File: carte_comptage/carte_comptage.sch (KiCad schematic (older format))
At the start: 40 parts, among them Q1 Si2302DS, U33 AP1117-33

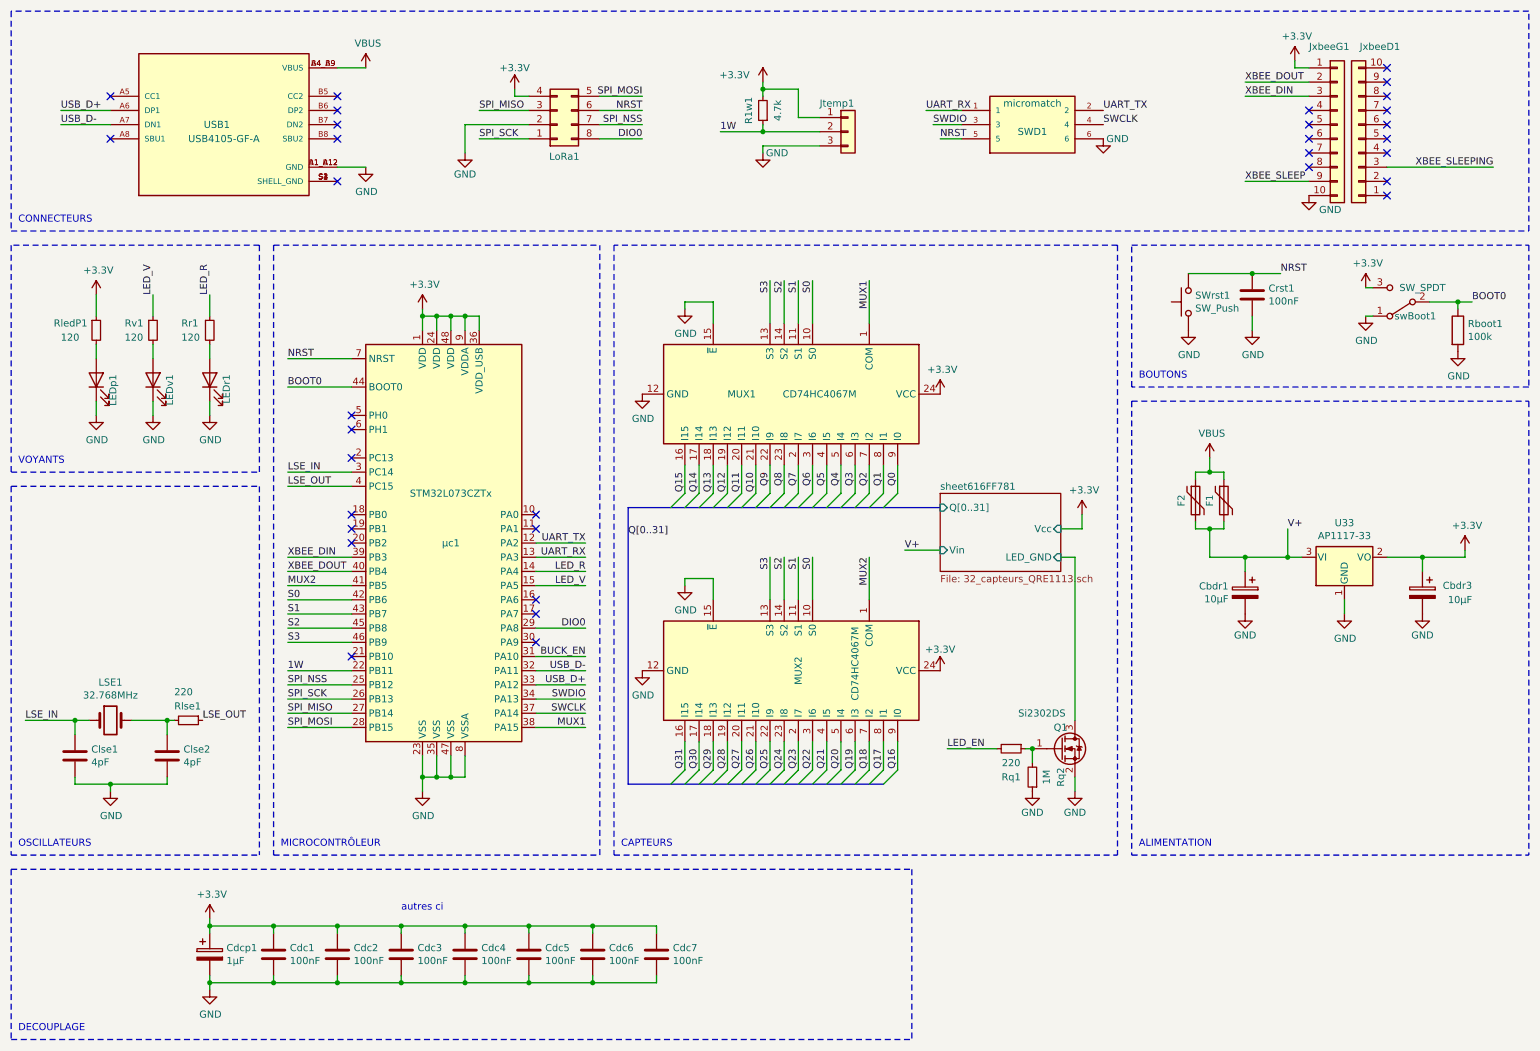
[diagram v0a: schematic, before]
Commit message: Routage fini, à vérifier, ajouter les encoches de montage
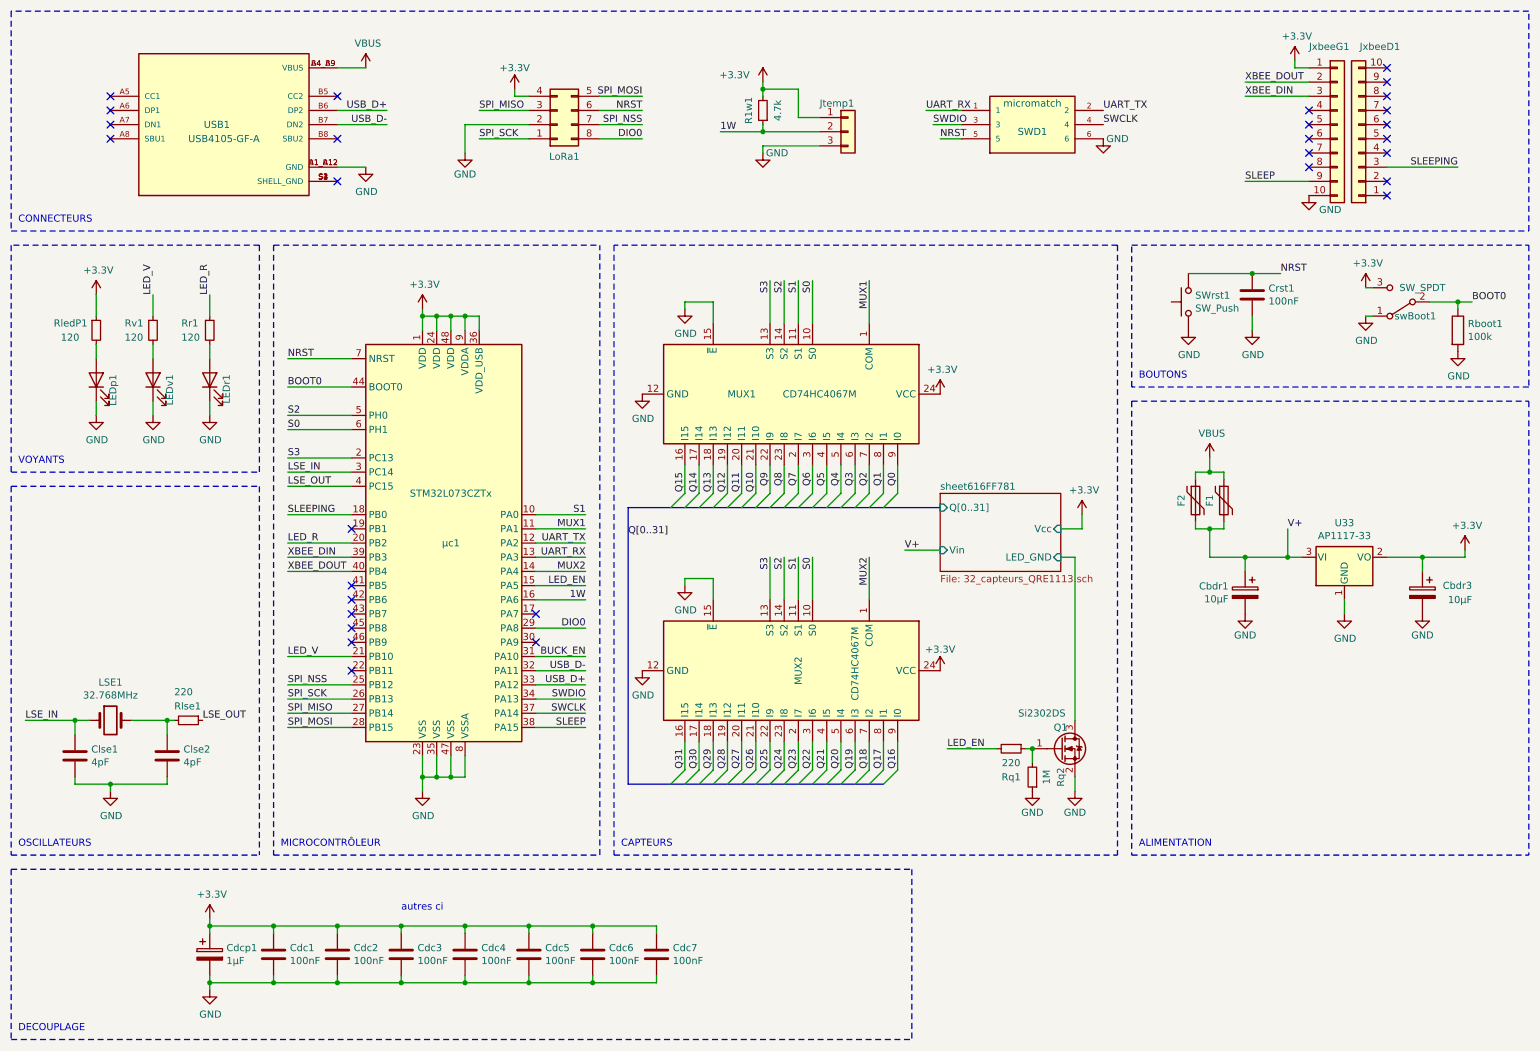
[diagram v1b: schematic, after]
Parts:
- Jtemp1: footprint Connector_JST:JST_EH_B3B-EH-A_1x03_P2.50mm_Vertical -> Connector_JST:JST_EH_S3B-EH_1x03_P2.50mm_Horizontal
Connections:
- net XBEE_SLEEPING is gone; now on net SLEEPING: JxbeeD1.3 (Pin_3)
- net 1W: now also µc1.16 (PA6); no longer µc1.22 (PB11)
- net LED_EN: now also µc1.15 (PA5)
- net LED_R: now also µc1.20 (PB2); no longer µc1.14 (PA4)
- net LED_V: now also µc1.21 (PB10); no longer µc1.15 (PA5)
- net MUX1: now also µc1.11 (PA1); no longer µc1.38 (PA15)
- net MUX2: now also µc1.14 (PA4); no longer µc1.41 (PB5)
- net S0: now also µc1.6 (PH1); no longer µc1.42 (PB6)
- net S1: now also µc1.10 (PA0); no longer µc1.43 (PB7)
- net S2: now also µc1.5 (PH0); no longer µc1.45 (PB8)
- net S3: now also µc1.2 (PC13); no longer µc1.46 (PB9)
- net USB_D+: now also USB1.B6 (DP2); no longer USB1.A6 (DP1)
- net USB_D-: now also USB1.B7 (DN2); no longer USB1.A7 (DN1)
- net SLEEPING: now reaches µc1.18 (PB0)
- net XBEE_SLEEP renamed SLEEP
- net SLEEP: now also µc1.38 (PA15)
- no-connect marks 33 -> 30
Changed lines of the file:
@@
 Wire Notes Line
 	500  2050 11200 2050
-Wire Wire Line
-	2450 5150 2900 5150
 Connection ~ 3400 5900
 Wire Wire Line
@@
 $EndComp
 Wire Wire Line
-	1200 1300 850  1300
-Wire Wire Line
-	850  1200 1200 1200
-Text Label 850  1300 0    50   ~ 0
+	2800 1300 3150 1300
+Wire Wire Line
+	3150 1200 2800 1200
+Text Label 3150 1300 2    50   ~ 0
 USB_D-
-Text Label 850  1200 0    50   ~ 0
+Text Label 3150 1200 2    50   ~ 0
 USB_D+
 Text Notes 8450 3100 0    50   ~ 0
@@
 NoConn ~ 1200 1100
 NoConn ~ 2800 1100
-NoConn ~ 2800 1200
-NoConn ~ 2800 1300
 $Comp
 L carte_comptage-rescue:USB4105-GF-A-USB4105-GF-A USB1
@@
 Wire Wire Line
 	9200 1100 9650 1100
-Text Label 10950 1600 2    50   ~ 0
-XBEE_SLEEPING
+Text Label 10700 1600 2    50   ~ 0
+SLEEPING
 Wire Notes Line
 	6850 6550 6850 7750
@@
 	2450 4450 2900 4450
 Text Label 9200 1700 0    50   ~ 0
-XBEE_SLEEP
+SLEEP
 Wire Wire Line
 	9200 1700 9650 1700
@@
 Wire Wire Line
 	2900 3850 2450 3850
-NoConn ~ 2900 3650
-Wire Wire Line
-	10950 1600 10200 1600
-NoConn ~ 4200 4750
-NoConn ~ 4200 4650
-NoConn ~ 2900 4050
-NoConn ~ 2900 4250
-NoConn ~ 2900 3350
-NoConn ~ 2900 3450
+Wire Wire Line
+	10700 1600 10200 1600
 Text Label 4950 1200 2    50   ~ 0
 NRST
@@
 Wire Wire Line
 	2450 5550 2900 5550
-NoConn ~ 4200 4050
-NoConn ~ 4200 4150
 Text Label 4550 4250 2    50   ~ 0
 UART_TX
 Text Label 4550 4350 2    50   ~ 0
 UART_RX
-Text Label 4550 4450 2    50   ~ 0
+Text Label 2450 4250 0    50   ~ 0
 LED_R
-Text Label 4550 4550 2    50   ~ 0
+Text Label 2450 5050 0    50   ~ 0
 LED_V
 Text Label 4550 5050 2    50   ~ 0
@@
 Wire Wire Line
 	2450 5250 2900 5250
-Text Label 2450 4650 0    50   ~ 0
+Text Label 2450 3450 0    50   ~ 0
 S0
-Text Label 2450 4850 0    50   ~ 0
+Text Label 2450 3350 0    50   ~ 0
 S2
-Text Label 2450 4950 0    50   ~ 0
+Text Label 2450 3650 0    50   ~ 0
 S3
-Text Label 2450 4750 0    50   ~ 0
+Text Label 4550 4050 2    50   ~ 0
 S1
-Wire Wire Line
-	2450 4650 2900 4650
-Wire Wire Line
-	2450 4750 2900 4750
-Wire Wire Line
-	2450 4850 2900 4850
-Wire Wire Line
-	2450 4950 2900 4950
-Text Label 2450 4550 0    50   ~ 0
+Text Label 4550 4450 2    50   ~ 0
 MUX2
-Wire Wire Line
-	2450 4550 2900 4550
-Text Label 4550 5550 2    50   ~ 0
+Text Label 4550 4150 2    50   ~ 0
 MUX1
 Wire Wire Line
@@
 Wire Wire Line
 	4550 4850 4200 4850
-NoConn ~ 2900 5050
-Text Label 2450 5150 0    50   ~ 0
+Text Label 4550 4650 2    50   ~ 0
 1W
 $Comp
@@
 F 0 "Jtemp1" H 6200 1550 50  0000 L CNN
 F 1 "Conn_01x03" H 6480 1301 50  0001 L CNN
-F 2 "Connector_JST:JST_EH_B3B-EH-A_1x03_P2.50mm_Vertical" H 6400 1350 50  0001 C CNN
+F 2 "Connector_JST:JST_EH_S3B-EH_1x03_P2.50mm_Horizontal" H 6400 1350 50  0001 C CNN
 F 3 "~" H 6400 1350 50  0001 C CNN
 	1    6400 1350
@@
 Text Label 4850 4200 0    50   ~ 0
 Q[0..31]
+Wire Wire Line
+	2450 3350 2900 3350
+Wire Wire Line
+	2900 3450 2450 3450
+Wire Wire Line
+	2450 3650 2900 3650
+Wire Wire Line
+	4200 4050 4550 4050
+Text Label 2450 4050 0    50   ~ 0
+SLEEPING
+Text Label 4550 5550 2    50   ~ 0
+SLEEP
+Wire Wire Line
+	4200 4150 4550 4150
+Wire Wire Line
+	2900 4250 2450 4250
+Wire Wire Line
+	2450 5050 2900 5050
+Wire Wire Line
+	2900 4050 2450 4050
+Wire Wire Line
+	4550 4650 4200 4650
+NoConn ~ 1200 1200
+NoConn ~ 1200 1300
+Text Label 4550 4550 2    50   ~ 0
+LED_EN
+NoConn ~ 2900 4550
+NoConn ~ 2900 4650
+NoConn ~ 2900 4750
+NoConn ~ 2900 4850
+NoConn ~ 2900 4950
+NoConn ~ 4200 4750
+NoConn ~ 2900 5150
 Wire Bus Line
 	4850 5950 6650 5950

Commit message: ajouter trous
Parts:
- removed SWD1: micromatch, 7-215079-6:TE_7-215079-6, symbol carte_comptage-rescue:7-215079-6-7-215079-6
- added SWD1: SWD, 7-188275-6:TE_7-188275-6, symbol 7-188275-6:7-188275-6
- Jtemp1: value Conn_01x03 -> 1 WIRE; footprint Connector_JST:JST_EH_S3B-EH_1x03_P2.50mm_Horizontal -> Connector_JST:JST_EH_B3B-EH-A_1x03_P2.50mm_Vertical
- JxbeeG1: value Conn_01x10 -> xBee
- SWrst1: value SW_Push -> RESET
- swBoot1: value SW_SPDT -> 0 boot 1
- renumbered Cdcp1 to C1, Cdc1 to C2, Cdc2 to C3, Cdc3 to C4, Cdc4 to C5, Cdc5 to C6, Cdc6 to C7, Cdc7 to C8, Cbdr1 to Cr1, Cbdr3 to Cr2, Rboot1 to Rb1
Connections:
- net GND: now also SWD1.6
- net NRST: now also SWD1.5
- net SWCLK: now also SWD1.4
- net SWDIO: now also SWD1.3
- net UART_RX: now also SWD1.1
- net UART_TX: now also SWD1.2
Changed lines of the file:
@@
 	5050 6950 5050 7000
 $Comp
-L Device:C Cdc7
+L Device:C C8
 U 1 1 6198EBF0
 P 5050 7150
-F 0 "Cdc7" H 5165 7196 50  0000 L CNN
+F 0 "C8" H 5165 7196 50  0000 L CNN
 F 1 "100nF" H 5165 7105 50  0000 L CNN
 F 2 "Capacitor_SMD:C_1206_3216Metric" H 5088 7000 50  0001 C CNN
@@
 $EndComp
 $Comp
-L Device:C Cdc6
+L Device:C C7
 U 1 1 6198E9CA
 P 4600 7150
-F 0 "Cdc6" H 4715 7196 50  0000 L CNN
+F 0 "C7" H 4715 7196 50  0000 L CNN
 F 1 "100nF" H 4715 7105 50  0000 L CNN
 F 2 "Capacitor_SMD:C_1206_3216Metric" H 4638 7000 50  0001 C CNN
@@
 	1900 6900 1900 6950
 $Comp
-L Device:C Cdc5
+L Device:C C6
 U 1 1 61341ED1
 P 4150 7150
-F 0 "Cdc5" H 4265 7196 50  0000 L CNN
+F 0 "C6" H 4265 7196 50  0000 L CNN
 F 1 "100nF" H 4265 7105 50  0000 L CNN
 F 2 "Capacitor_SMD:C_1206_3216Metric" H 4188 7000 50  0001 C CNN
@@
 $EndComp
 $Comp
-L Device:C Cdc4
+L Device:C C5
 U 1 1 6132D2C5
 P 3700 7150
-F 0 "Cdc4" H 3815 7196 50  0000 L CNN
+F 0 "C5" H 3815 7196 50  0000 L CNN
 F 1 "100nF" H 3815 7105 50  0000 L CNN
 F 2 "Capacitor_SMD:C_1206_3216Metric" H 3738 7000 50  0001 C CNN
@@
 $EndComp
 $Comp
-L Device:C Cdc3
+L Device:C C4
 U 1 1 6132C7CA
 P 3250 7150
-F 0 "Cdc3" H 3365 7196 50  0000 L CNN
+F 0 "C4" H 3365 7196 50  0000 L CNN
 F 1 "100nF" H 3365 7105 50  0000 L CNN
 F 2 "Capacitor_SMD:C_1206_3216Metric" H 3288 7000 50  0001 C CNN
@@
 $EndComp
 $Comp
-L Device:C Cdc2
+L Device:C C3
 U 1 1 6132C2F1
 P 2800 7150
-F 0 "Cdc2" H 2915 7196 50  0000 L CNN
+F 0 "C3" H 2915 7196 50  0000 L CNN
 F 1 "100nF" H 2915 7105 50  0000 L CNN
 F 2 "Capacitor_SMD:C_1206_3216Metric" H 2838 7000 50  0001 C CNN
@@
 $EndComp
 $Comp
-L Device:CP Cdcp1
+L Device:CP C1
 U 1 1 613252A0
 P 1900 7150
-F 0 "Cdcp1" H 2018 7196 50  0000 L CNN
+F 0 "C1" H 2018 7196 50  0000 L CNN
 F 1 "1µF" H 2018 7105 50  0000 L CNN
 F 2 "Capacitor_SMD:C_1206_3216Metric" H 1938 7000 50  0001 C CNN
@@
 $EndComp
 $Comp
-L Device:C Cdc1
+L Device:C C2
 U 1 1 6132462D
 P 2350 7150
-F 0 "Cdc1" H 2465 7196 50  0000 L CNN
+F 0 "C2" H 2465 7196 50  0000 L CNN
 F 1 "100nF" H 2465 7105 50  0000 L CNN
 F 2 "Capacitor_SMD:C_1206_3216Metric" H 2388 7000 50  0001 C CNN
@@
 	10700 2550 10700 2600
 $Comp
-L Device:R Rboot1
+L Device:R Rb1
 U 1 1 6135D4F7
 P 10700 2750
-F 0 "Rboot1" H 10770 2796 50  0000 L CNN
+F 0 "Rb1" H 10770 2796 50  0000 L CNN
 F 1 "100k" H 10770 2705 50  0000 L CNN
 F 2 "Resistor_SMD:R_1206_3216Metric" V 10630 2750 50  0001 C CNN
@@
 P 10300 2550
 F 0 "swBoot1" H 10200 2650 50  0000 C CNN
-F 1 "SW_SPDT" H 10150 2450 50  0000 C CNN
+F 1 "0 boot 1" H 10150 2450 50  0000 C CNN
 F 2 "Button_Switch_THT:SW_Slide_1P2T_CK_OS102011MS2Q" H 10300 2550 50  0001 C CNN
 F 3 "~" H 10300 2550 50  0001 C CNN
@@
 P 8800 2550
 F 0 "SWrst1" V 8846 2502 50  0000 R CNN
-F 1 "SW_Push" V 8755 2502 50  0000 R CNN
+F 1 "RESET" V 8755 2502 50  0000 R CNN
 F 2 "Button_Switch_SMD:SW_SPST_TL3305C" H 8800 2750 50  0001 C CNN
 F 3 "~" H 8800 2750 50  0001 C CNN
@@
 $EndComp
 $Comp
-L carte_comptage-rescue:7-215079-6-7-215079-6 SWD1
-U 1 1 613584C4
-P 7700 1300
-F 0 "SWD1" H 7700 1250 50  0000 C CNN
-F 1 "micromatch" H 7700 1450 50  0000 C CNN
-F 2 "7-215079-6:TE_7-215079-6" H 7700 1300 50  0001 L BNN
-F 3 "" H 7700 1300 50  0001 L BNN
-F 4 "7-215079-6" H 7700 1300 50  0001 L BNN "Comment"
-	1    7700 1300
-	1    0    0    -1
-$EndComp
-$Comp
 L power:GND #PWR029
 U 1 1 61359D10
-P 8200 1400
-F 0 "#PWR029" H 8200 1150 50  0001 C CNN
-F 1 "GND" H 8300 1400 50  0000 C CNN
-F 2 "" H 8200 1400 50  0001 C CNN
-F 3 "" H 8200 1400 50  0001 C CNN
-	1    8200 1400
-	1    0    0    -1
-$EndComp
-Text Label 7050 1400 0    50   ~ 0
+P 7350 1550
+F 0 "#PWR029" H 7350 1300 50  0001 C CNN
+F 1 "GND" H 7200 1600 50  0000 C CNN
+F 2 "" H 7350 1550 50  0001 C CNN
+F 3 "" H 7350 1550 50  0001 C CNN
+	1    7350 1550
+	1    0    0    -1
+$EndComp
+Text Label 8550 1400 2    50   ~ 0
 NRST
-Wire Wire Line
-	7050 1400 7200 1400
-Text Label 7000 1300 0    50   ~ 0
+Text Label 8550 1200 2    50   ~ 0
 SWDIO
-Wire Wire Line
-	7000 1300 7200 1300
-Text Label 8200 1300 0    50   ~ 0
+Text Label 7050 1300 0    50   ~ 0
 SWCLK
-Text Label 8200 1200 0    50   ~ 0
+Text Label 7050 1100 0    50   ~ 0
 UART_TX
-Text Label 6950 1200 0    50   ~ 0
+Text Label 8550 1000 2    50   ~ 0
 UART_RX
-Wire Wire Line
-	6950 1200 7200 1200
 Wire Notes Line
 	11200 2050 11200 500
@@
 P 9850 1300
 F 0 "JxbeeG1" H 9650 1850 50  0000 L CNN
-F 1 "Conn_01x10" H 9930 1201 50  0001 L CNN
+F 1 "xBee" H 9930 1201 50  0001 L CNN
 F 2 "Connector_PinSocket_2.00mm:PinSocket_1x10_P2.00mm_Vertical" H 9850 1300 50  0001 C CNN
 F 3 "~" H 9850 1300 50  0001 C CNN
@@
 P 6400 1350
 F 0 "Jtemp1" H 6200 1550 50  0000 L CNN
-F 1 "Conn_01x03" H 6480 1301 50  0001 L CNN
-F 2 "Connector_JST:JST_EH_S3B-EH_1x03_P2.50mm_Horizontal" H 6400 1350 50  0001 C CNN
+F 1 "1 WIRE" H 6480 1301 50  0001 L CNN
+F 2 "Connector_JST:JST_EH_B3B-EH-A_1x03_P2.50mm_Vertical" H 6400 1350 50  0001 C CNN
 F 3 "~" H 6400 1350 50  0001 C CNN
 	1    6400 1350
@@
 	6800 4300 7050 4300
 $Comp
-L Device:CP Cbdr1
+L Device:CP Cr1
 U 1 1 619142CD
 P 9200 4600
-F 0 "Cbdr1" H 9318 4646 50  0000 L CNN
+F 0 "Cr1" H 9318 4646 50  0000 L CNN
 F 1 "10µF" H 9318 4555 50  0000 L CNN
 F 2 "Capacitor_Tantalum_SMD:CP_EIA-3216-18_Kemet-A" H 9238 4450 50  0001 C CNN
@@
 $EndComp
 $Comp
-L Device:CP Cbdr3
+L Device:CP Cr2
 U 1 1 61931D9B
 P 10450 4600
-F 0 "Cbdr3" H 10100 4650 50  0000 L CNN
+F 0 "Cr2" H 10100 4650 50  0000 L CNN
 F 1 "10µF" H 10100 4550 50  0000 L CNN
 F 2 "Capacitor_Tantalum_SMD:CP_EIA-3216-18_Kemet-A" H 10488 4450 50  0001 C CNN
@@
 U 1 1 616E94D9
 P 6050 5150
-F 0 "MUX2" H 6050 5150 50  0000 C CNN
-F 1 "CD74HC4067M" H 6000 5550 50  0000 C CNN
+F 0 "MUX2" V 6050 4700 50  0000 C CNN
+F 1 "CD74HC4067M" V 6050 5350 50  0000 C CNN
 F 2 "Package_SO:SOIC-24W_7.5x15.4mm_P1.27mm" H 6950 4150 50  0001 C CIN
 F 3 "http://www.ti.com/lit/ds/symlink/cd74hc4067.pdf" H 5700 6000 50  0001 C CNN
@@
 NoConn ~ 4200 4750
 NoConn ~ 2900 5150
+$Comp
+L 7-188275-6:7-188275-6 SWD1
+U 1 1 61594CE4
+P 7800 1200
+F 0 "SWD1" H 7800 1575 50  0000 C CNN
+F 1 "SWD" H 7800 1576 50  0001 C CNN
+F 2 "7-188275-6:TE_7-188275-6" H 7800 1200 50  0001 L BNN
+F 3 "" H 7800 1200 50  0001 L BNN
+F 4 "7-188275-6" H 7800 1200 50  0001 L BNN "Comment"
+	1    7800 1200
+	1    0    0    -1
+$EndComp
+Wire Wire Line
+	8550 1400 8200 1400
+Wire Wire Line
+	8200 1200 8550 1200
+Wire Wire Line
+	8550 1000 8200 1000
+Wire Wire Line
+	7400 1100 7050 1100
+Wire Wire Line
+	7050 1300 7400 1300
+Wire Wire Line
+	7400 1500 7350 1500
+Wire Wire Line
+	7350 1500 7350 1550
 Wire Bus Line
 	4850 5950 6650 5950

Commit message: fonctionne à nouveau
programmation automatique du xBee
routeurs envoient l’alerte au coordinateur
signal lumineux alerte si on reçoit une alerte
réparé le buffer de lecture --> lit du premier coup au lieux du deuxieme
(à étudier si c'est pas intéressant de faire des alertes récurrentes jusqu'à un acknowledge plutôt qu'une seule, au cas où elle est pas passée)
reset à distance
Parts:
- SWD1: symbol 7-188275-6:7-188275-6 -> carte_comptage-rescue:7-188275-6-7-188275-6
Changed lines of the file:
@@
 NoConn ~ 2900 5150
 $Comp
-L 7-188275-6:7-188275-6 SWD1
+L carte_comptage-rescue:7-188275-6-7-188275-6 SWD1
 U 1 1 61594CE4
 P 7800 1200
